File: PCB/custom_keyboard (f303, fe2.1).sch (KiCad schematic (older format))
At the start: 440 parts, among them IC1 FE2.1, J2 Conn_01x03_Male, J5 AVR-ISP-6, Q1 DTC123J, SW1 SW_Push, U1 24LC02BT-I/SN, U10 PRTR5V0U2X, U11 XC6206P332MR, U12 74LVC1G34, U13 XC6206P332MR, U14 MIC2505, U15 MIC2505, U2 PRTR5V0U2X, U3 PRTR5V0U2X, U4 PRTR5V0U2X, U5 PRTR5V0U2X, U6 PRTR5V0U2X, U7 PRTR5V0U2X, U8 PRTR5V0U2X, U9 STM32F303CBT6, Y1 8MHz, Y2 32.768KHz, Y3 12MHz

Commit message: Fixed JLCPCB BOM file not generating
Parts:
- H1, H2, H3, H4, J5, MX1, MX10, MX11, MX12, MX13, MX14, MX15, MX16, MX17, MX18, MX19, MX2, MX20, MX21, MX22, MX23, MX24, MX25, MX26, MX27, MX28, MX29, MX3, MX30, MX31, MX32, MX33, MX34, MX35, MX36, MX37, MX38, MX39, MX4, MX40, MX41, MX42, MX43, MX44, MX45, MX46, MX47, MX48, MX49, MX5, MX50, MX51, MX52, MX53, MX54, MX55, MX56, MX57, MX58, MX59, MX6, MX60, MX61, MX62, MX63, MX64, MX65, MX66, MX67, MX68, MX69, MX7, MX70, MX71, MX72, MX73, MX74, MX75, MX76, MX77, MX78, MX79, MX8, MX80, MX81, MX82, MX83, MX84, MX85, MX86, MX87, MX88, MX89, MX9, MX90, OL1, ROT1, ROT2, TP1, TP2, TP3, TP4: JLCPCB BOM (none) -> 0
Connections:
- net +3V3: no longer C41.1, U11.2 (VO)
- net PORT1-4_PWR: no longer U14.6 (OUT)
- net PORT5-7PWR: no longer U15.6 (OUT)
- new net: C41.1, U11.2 (VO)
- no-connect marks 9 -> 11

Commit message: Addressed several issues with power
- Rearranged downstream ports so that the fuse is positioned better
- Added ferrite beads to downstream ports
- Added fuse to LED matrix
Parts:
- added FB10, FB11, FB12, FB13, FB14, FB15, FB9: 60 @ 100 MHz, Inductor_SMD:L_0805_2012Metric, symbol Device:Ferrite_Bead_Small
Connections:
- net +3V3: now also C41.1, R50.1, U11.2 (VO); no longer R50.2
- net +5V: now also R13.1, R15.1, R39.1, R48.1; no longer F1.1, F1.2, R13.2, R15.2, R39.2, R42.1, R48.2, U10.4 (VCC), U3.4 (VCC), U4.4 (VCC), U5.4 (VCC), U6.4 (VCC), U7.4 (VCC), U8.4 (VCC)
- net GND: now also C1.2, C3.2, C32.2, C33.2, C4.2, C9.2; no longer C1.1, C3.1, C32.1, C33.1, C4.1, C9.1
- net HUB_XIN: now also C32.1; no longer C32.2
- net HUB_XOUT: now also C33.1; no longer C33.2
- net KEYBOARD_SDA: now also R50.2; no longer R50.1
- net KEYBOARD_XTAL1: now also C1.1; no longer C1.2
- net PORT1-4_PWR: now also F1.1, F1.2, R42.1, U10.4 (VCC), U14.6 (OUT), U6.4 (VCC), U7.4 (VCC), U8.4 (VCC), FB10.1, FB10.2, FB11.1, FB11.2, FB15.1, FB15.2, FB9.1, FB9.2
- net PORT5-7PWR: now also U15.6 (OUT), U3.4 (VCC), U4.4 (VCC), U5.4 (VCC), FB12.1, FB12.2, FB13.1, FB13.2, FB14.1, FB14.2
- net USB_XTAL1: now also C4.1; no longer C4.2
- net at R5.2, Y1.3: now also C3.1; no longer C3.2
- net at C5.2, R12.1, ROT1.A: now also R13.2; no longer R13.1
- net at C6.1, R40.2, ROT1.B: now also R48.2; no longer R48.1
- net at C7.2, R14.1, ROT2.A: now also R39.2; no longer R39.1
- net at C8.1, R49.2, ROT2.B: now also R15.2; no longer R15.1
- net at R16.2, Y2.2: now also C9.1; no longer C9.2
- net at R10.1, USB5.10 (CC2): no longer R11.1, USB5.4 (CC1)
- net at R28.1, USB7.4 (CC1): no longer R27.1, USB7.10 (CC2)
- net at R36.1, USB2.4 (CC1): no longer R35.1, USB2.10 (CC2)
- net at R8.1, USB1.10 (CC2): no longer R9.1, USB1.4 (CC1)
- new net: R11.1, USB5.4 (CC1)
- new net: R27.1, USB7.10 (CC2)
- new net: R35.1, USB2.10 (CC2)
- new net: R9.1, USB1.4 (CC1)
- no-connect marks 11 -> 9
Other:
- note added: "LED 3.3V to 5V"
- note removed: "LED Power"
- moved on the sheet: C11, C12, C14, C15, C22, C24, C25, C26, C27, C28, C29, C30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

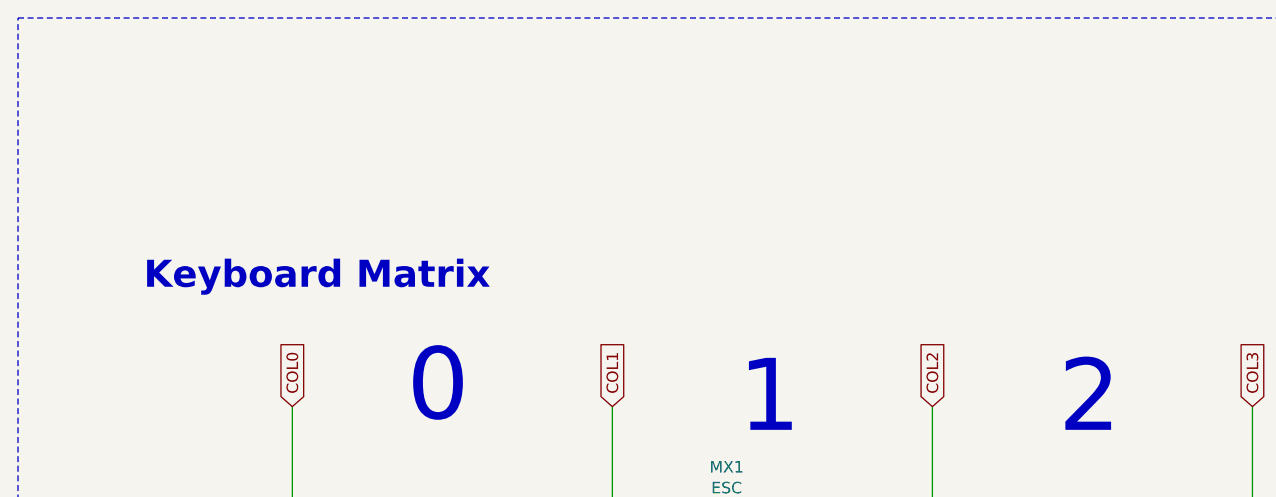
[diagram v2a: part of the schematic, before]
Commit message: Rearranged vias
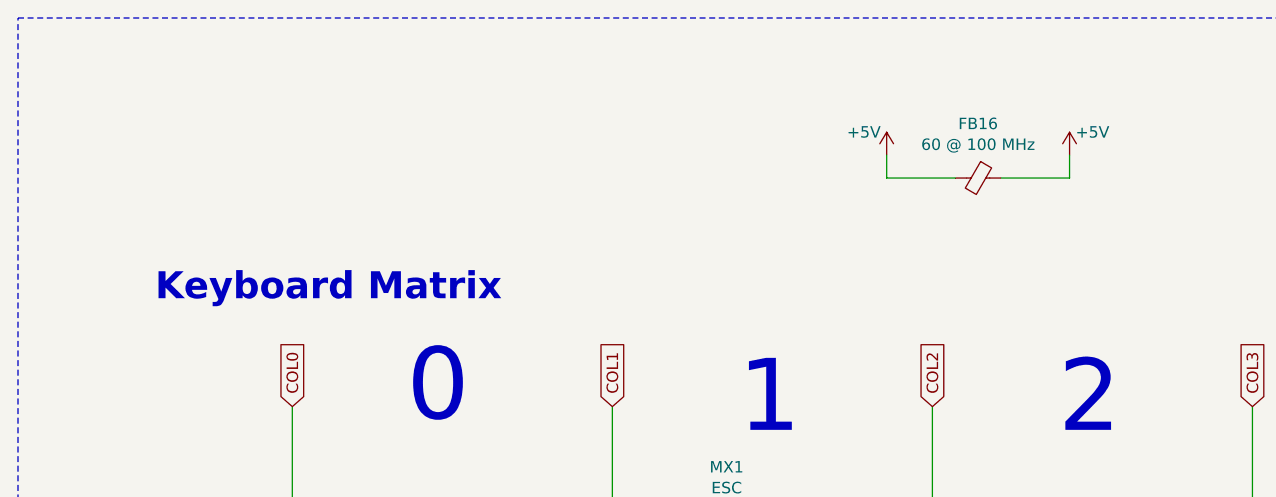
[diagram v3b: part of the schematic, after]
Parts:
- added FB16: 60 @ 100 MHz, Inductor_SMD:L_0805_2012Metric, symbol Device:Ferrite_Bead_Small
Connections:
- net +5V: now also FB16.1, FB16.2
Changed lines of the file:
@@
 Text GLabel 3650 4250 0    50   Input ~ 0
 ROW0
-Text Notes 3500 2600 0    118  ~ 24
+Text Notes 3550 2650 0    118  ~ 24
 Keyboard Matrix
 Text Notes 16200 2000 0    276  ~ 55
@@
 Wire Wire Line
 	4650 21050 4600 21050
+$Comp
+L Device:Ferrite_Bead_Small FB16
+U 1 1 CAF4EC3C
+P 7150 2100
+F 0 "FB16" V 6913 2100 50  0000 C CNN
+F 1 "60 @ 100 MHz" V 7004 2100 50  0000 C CNN
+F 2 "Inductor_SMD:L_0805_2012Metric" V 7080 2100 50  0001 C CNN
+F 3 "~" H 7150 2100 50  0001 C CNN
+	1    7150 2100
+	0    1    1    0
+$EndComp
+$Comp
+L power:+5V #PWR094
+U 1 1 CAF4FFC3
+P 7550 2000
+F 0 "#PWR094" H 7550 1850 50  0001 C CNN
+F 1 "+5V" H 7650 2100 50  0000 C CNN
+F 2 "" H 7550 2000 50  0001 C CNN
+F 3 "" H 7550 2000 50  0001 C CNN
+	1    7550 2000
+	1    0    0    -1
+$EndComp
+$Comp
+L power:+5V #PWR093
+U 1 1 CAF54A00
+P 6750 2000
+F 0 "#PWR093" H 6750 1850 50  0001 C CNN
+F 1 "+5V" H 6850 2100 50  0000 C CNN
+F 2 "" H 6750 2000 50  0001 C CNN
+F 3 "" H 6750 2000 50  0001 C CNN
+	1    6750 2000
+	-1   0    0    -1
+$EndComp
+Wire Wire Line
+	7050 2100 6750 2100
+Wire Wire Line
+	6750 2100 6750 2000
+Wire Wire Line
+	7550 2100 7550 2000
+Wire Wire Line
+	7250 2100 7550 2100
 $EndSCHEMATC
